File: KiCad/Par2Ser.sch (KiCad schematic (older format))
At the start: 34 parts, among them J1 DB25_Male, J2 Arduino UART header, J3 USB_C_Receptacle_USB2.0, J4 Conn_01x02, Q1 BC857, U1 Arduino_Nano_V3, U2 FT232RNL-REEL, U3 SC16IS750IBS,128, X1 Abracon-ASFL1-7.3728MHZ-EK-T

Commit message: Add LC4032V-5TN48C CPLD and remove Arduino Nano
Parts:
- removed JP1: PinHeader for 2mm Shunt Jumper, Connector_PinHeader_2.00mm:PinHeader_1x02_P2.00mm_Vertical, symbol Connector_Generic:Conn_01x02
- removed U1: Arduino_Nano_V3, Par2Ser:Arduino_Nano_V3, symbol Par2Ser:Arduino_Nano_V3
- added U4: LC4032V-5TN48C, Package_QFP:TQFP-48_7x7mm_P0.5mm, symbol Par2Ser:LC4032V-5TN48C
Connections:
- net labels added: 1V8, TCK, TD0, TDI, TMS
- net labels removed: Amiga_RESET
- wire segments 75 -> 73
- no-connect marks 26 -> 20
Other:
- moved on the sheet: C3, C4, C5, C6, C7, R6, RN1, RN2, U2

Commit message: Remove unused components and begin pin assigment on CPLD, place and route pull-up resistor networks and series resistor networks for parallel port signals
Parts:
- removed J2: Arduino UART header, Par2Ser:PinSocket_1x02_P2.54mm_SMD, symbol Connector_Generic:Conn_01x02
- removed J4: Conn_01x02, Par2Ser:PinSocket_1x02_P2.54mm_SMD, symbol Connector_Generic:Conn_01x02
- removed Q1: BC857, Package_TO_SOT_SMD:SOT-23_Handsoldering, symbol Transistor_BJT:BC857
- removed R5: 4k7, Resistor_SMD:R_1206_3216Metric_Pad1.30x1.75mm_HandSolder, symbol Device:R_Small
- removed RN2: 10k, Resistor_THT:R_Array_SIP9, symbol Device:R_Network08
- removed U3: SC16IS750IBS,128, Par2Ser:HVQFN-24-1EP_4x4mm_P0.5mm_EP2.6x2.6mm_HandSolder, symbol Par2Ser:SC16IS750IBS,128
- removed X1: Abracon-ASFL1-7.3728MHZ-EK-T, Oscillator:Oscillator_SMD_SeikoEpson_SG8002LB-4Pin_5.0x3.2mm, symbol Par2Ser:Abracon-ASFL1-7.3728MHZ-EK-T
- added RN2: 10k, Resistor_THT:R_Array_SIP5, symbol Device:R_Network04
- added RN3, RN4, RN5: 330, Resistor_SMD:R_Array_Convex_4x0603, symbol Device:R_Pack04
- added U3: FT240XS-R, Par2Ser:SOP64P599X175-24N, symbol Par2Ser:FT240XS-R
- R6: value 1k 0805 -> 330
- renumbered J3 to J2, U4 to U1
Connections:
- net labels added: BUSY_B9, D0_3V3, D0_B0, D1_3V3, D1_B1, D2_3V3, D2_B2, D3_3V3, D3_B3, D4_3V3, D4_B4, D5_3V3, D5_B5, D6_3V3, D6_B6, D7_3V3, D7_B7, POUT_B10, SELECT_B11, STRB
- net labels removed: 1V8, 7M, Base, Collector, MISO, MOSI, RX0, SCK, SS, TX0
- wire segments 73 -> 70
- no-connect marks 20 -> 16
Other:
- note removed: "Bottom"
- note removed: "Top"
- moved on the sheet: C3, C4, C5, C6, C7, D1, R1, R6, U2

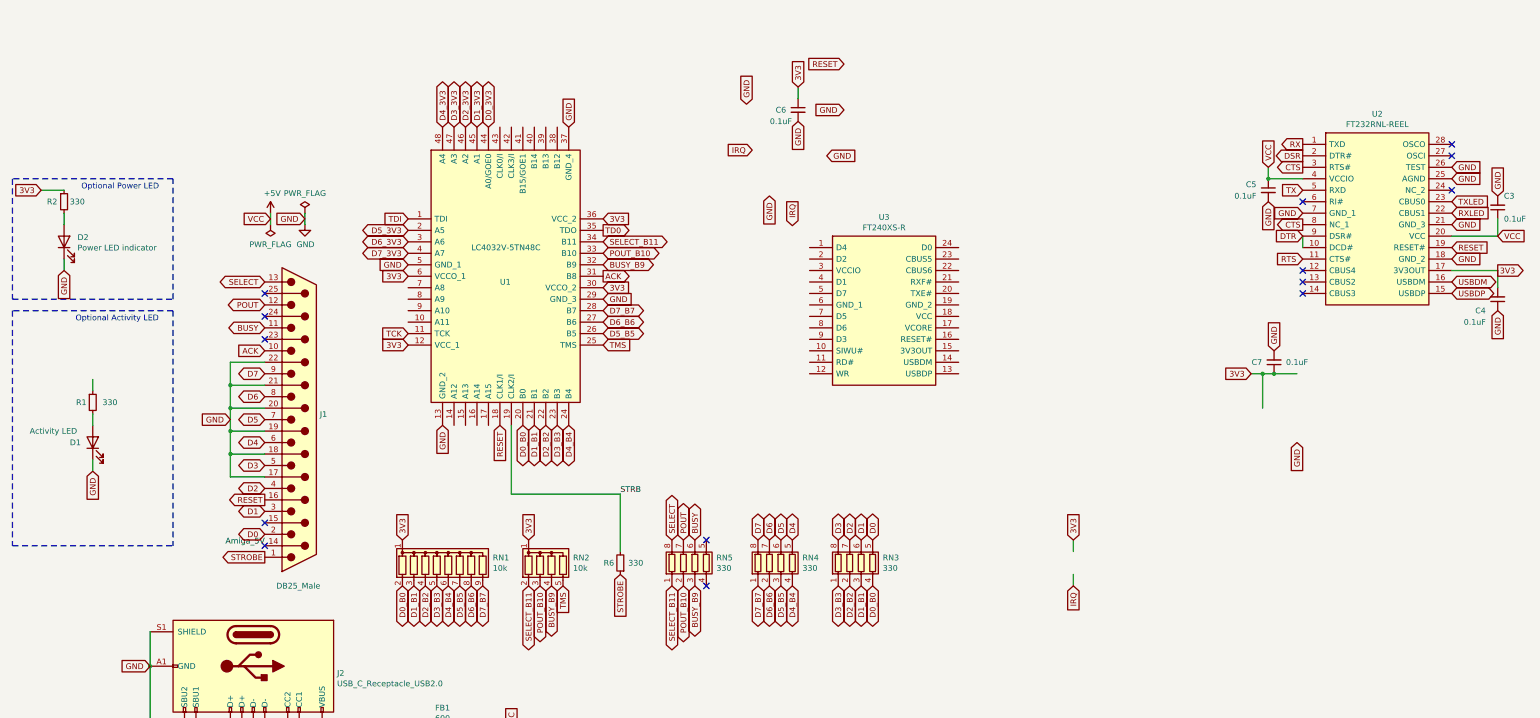
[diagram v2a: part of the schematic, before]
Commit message: Replace FT232RNL with FT240X and do some routing
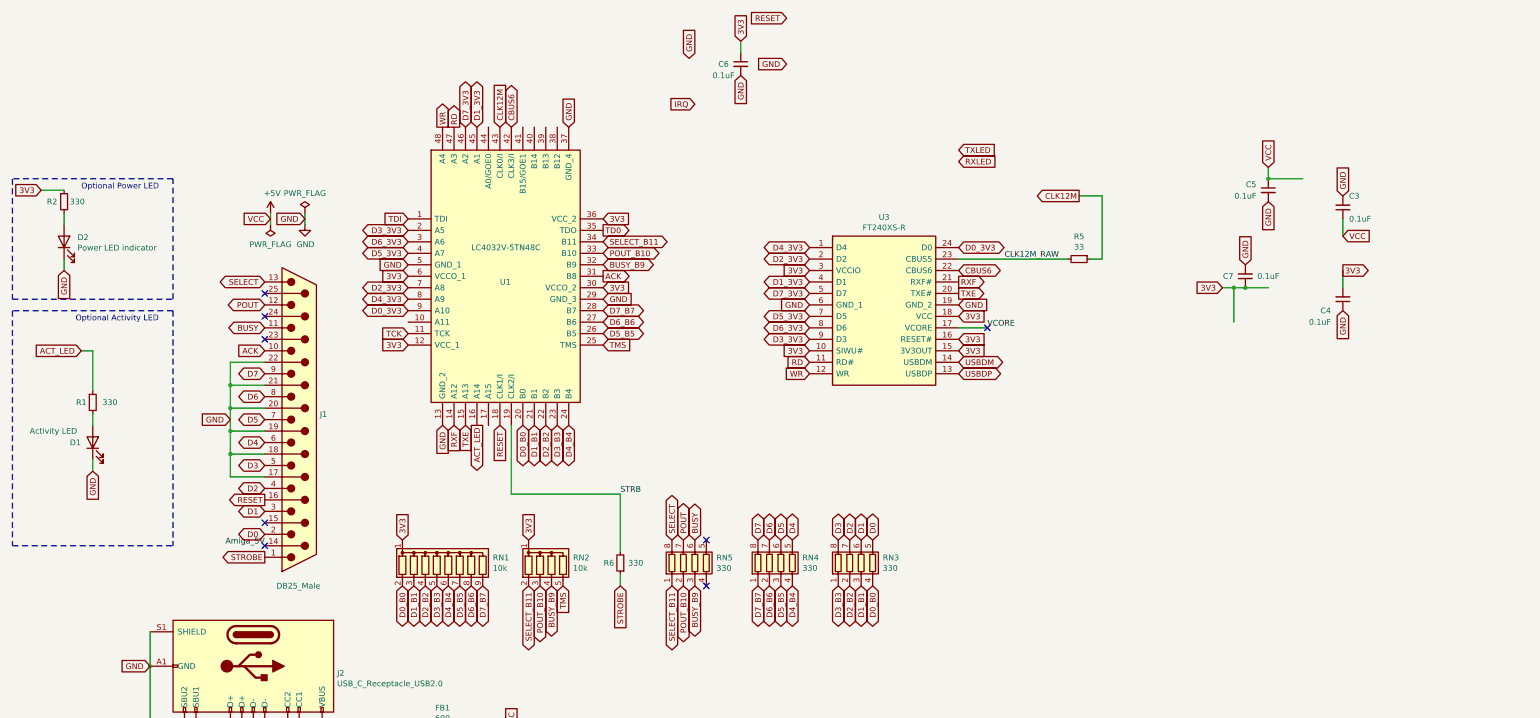
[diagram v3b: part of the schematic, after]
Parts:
- removed U2: FT232RNL-REEL, Package_SO:SSOP-28_5.3x10.2mm_P0.65mm, symbol Par2Ser:FT232RNL-REEL
- added R5: 33, Resistor_SMD:R_0603_1608Metric_Pad0.98x0.95mm_HandSolder, symbol Device:R_Small
- U3: footprint Par2Ser:SOP64P599X175-24N -> Package_SO:SSOP-24_3.9x8.7mm_P0.635mm
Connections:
- net labels added: ACT_LED, CBUS6, CLK12M, CLK12M_RAW, RD, RXF, TXE, VCORE, WR
- net labels removed: CTS, DSR, DTR, RTS, RX, TX
- wire segments 70 -> 72
- no-connect marks 16 -> 10
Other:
- moved on the sheet: C3, C4, C6, C7

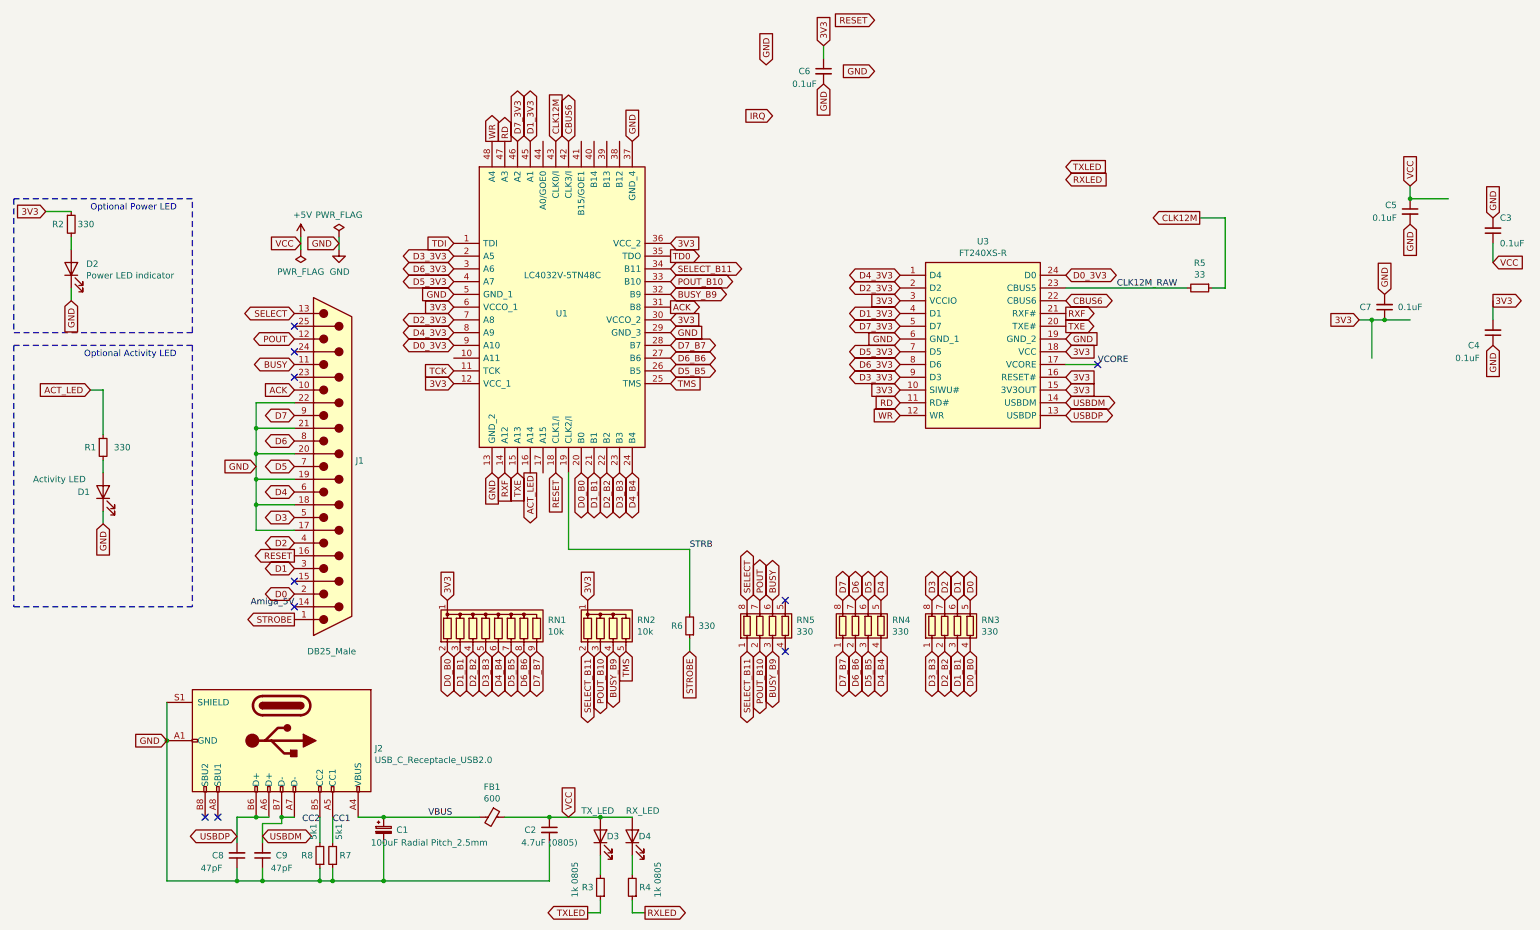
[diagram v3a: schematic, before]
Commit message: Fix placement and routing of caps and resistors
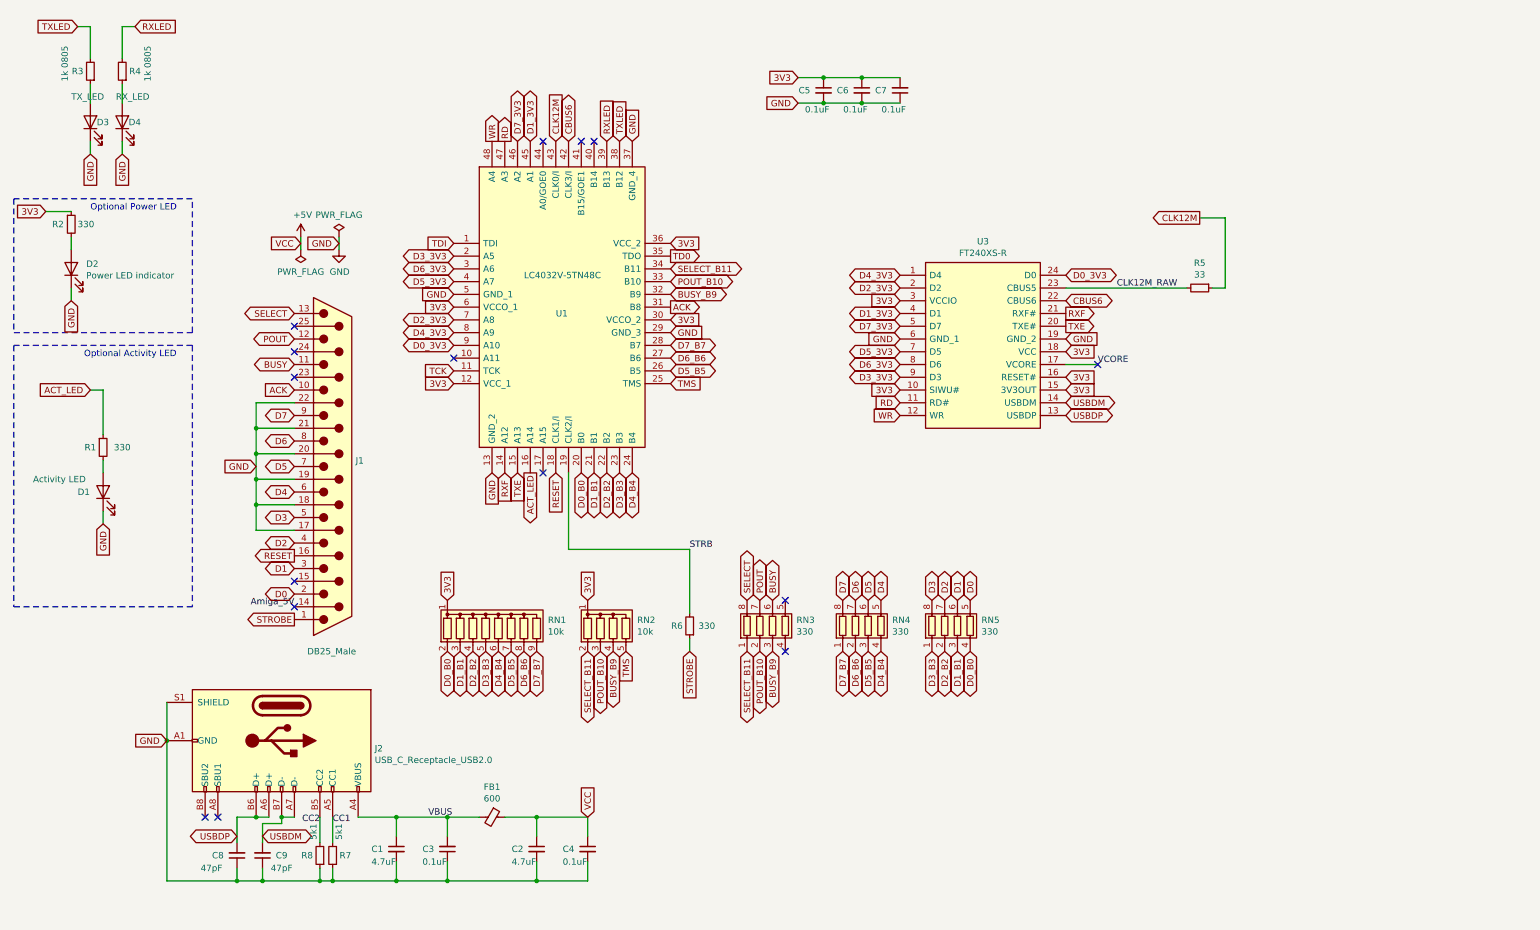
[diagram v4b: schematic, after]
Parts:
- removed C1: 100uF Radial Pitch_2.5mm, Capacitor_THT:CP_Radial_D5.0mm_P2.50mm, symbol Device:CP_Small
- added C1: 4.7uF, Capacitor_SMD:C_0805_2012Metric_Pad1.18x1.45mm_HandSolder, symbol Device:C_Small
- C2: value 4.7uF (0805) -> 4.7uF
- C6: footprint Capacitor_SMD:C_0805_2012Metric_Pad1.18x1.45mm_HandSolder -> Capacitor_SMD:C_0603_1608Metric_Pad1.08x0.95mm_HandSolder
- R1, R2, R7, R8: footprint Resistor_SMD:R_1206_3216Metric_Pad1.30x1.75mm_HandSolder -> Resistor_SMD:R_0805_2012Metric_Pad1.20x1.40mm_HandSolder
- renumbered C4 to C3, C5 to C4, C3 to C5, RN5 to RN3, RN3 to RN5
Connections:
- net labels removed: IRQ
- wire segments 72 -> 79
- no-connect marks 10 -> 15
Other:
- moved on the sheet: C2, C3, C4, C5, C6, C7, D3, D4, R3, R4

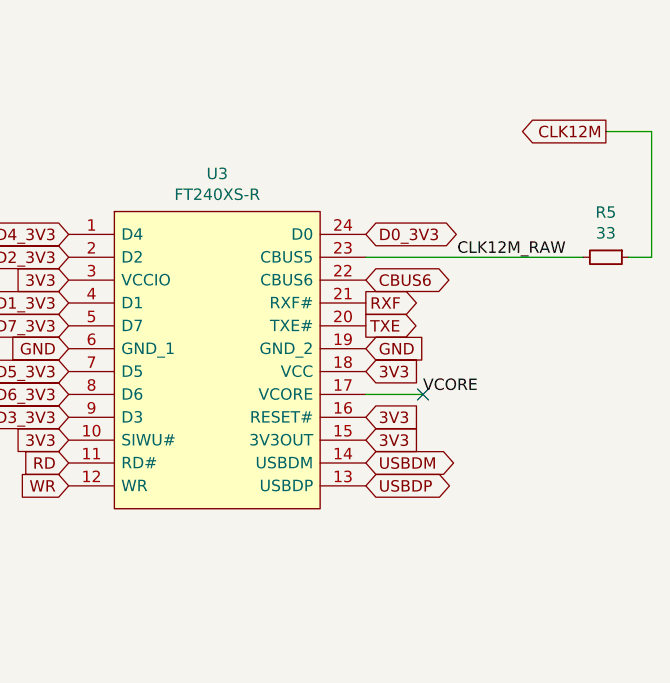
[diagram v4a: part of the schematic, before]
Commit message: Add resistors on the two USB data lines
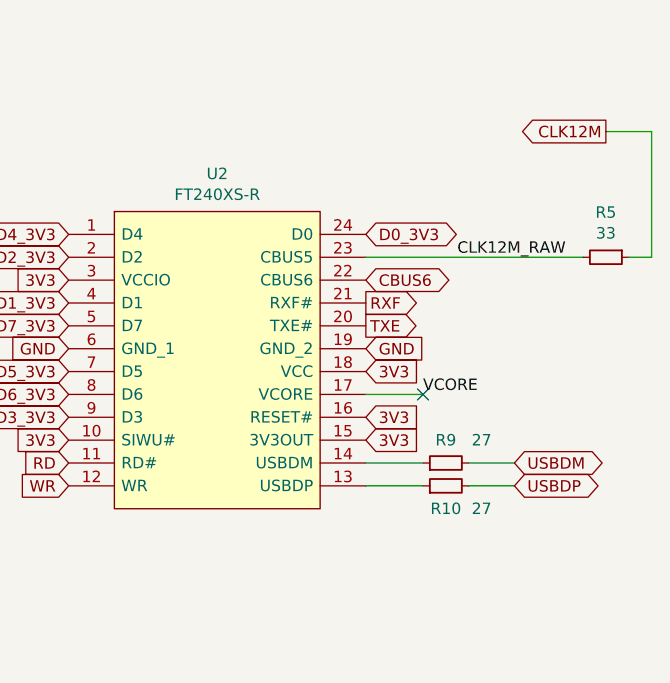
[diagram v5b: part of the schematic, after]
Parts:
- added R10, R9: 27, Resistor_SMD:R_0805_2012Metric_Pad1.20x1.40mm_HandSolder, symbol Device:R_Small
- renumbered U3 to U2
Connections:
- net USBDM: now also R9.2; no longer U2.14 (USBDM)
- net USBDP: now also R10.2; no longer U2.13 (USBDP)
- new net: R10.1, U2.13 (USBDP)
- new net: R9.1, U2.14 (USBDM)
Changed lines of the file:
@@
 D7_3V3
 $Comp
-L Par2Ser:FT240XS-R U3
+L Par2Ser:FT240XS-R U2
 U 1 1 6A22D05C
 P 9150 3250
-F 0 "U3" H 9150 4065 50  0000 C CNN
+F 0 "U2" H 9150 4065 50  0000 C CNN
 F 1 "FT240XS-R" H 9150 3974 50  0000 C CNN
 F 2 "Package_SO:SSOP-24_3.9x8.7mm_P0.635mm" H 8900 3950 50  0001 L CNN
@@
 Text GLabel 9800 3200 2    50   Input ~ 0
 GND
-Text GLabel 9800 3700 2    50   BiDi ~ 0
+Text GLabel 10450 3700 2    50   BiDi ~ 0
 USBDM
-Text GLabel 9800 3800 2    50   BiDi ~ 0
+Text GLabel 10450 3800 2    50   BiDi ~ 0
 USBDP
 Text GLabel 9800 3600 2    50   Input ~ 0
@@
 Wire Wire Line
 	2400 1200 2400 1350
+$Comp
+L Device:R_Small R10
+U 1 1 6A5B4EB2
+P 10150 3800
+F 0 "R10" V 10050 3800 50  0000 C CNN
+F 1 "27" V 10050 3600 50  0000 L CNN
+F 2 "Resistor_SMD:R_0805_2012Metric_Pad1.20x1.40mm_HandSolder" H 10150 3800 50  0001 C CNN
+F 3 "~" H 10150 3800 50  0001 C CNN
+	1    10150 3800
+	0    -1   -1   0
+$EndComp
+$Comp
+L Device:R_Small R9
+U 1 1 6A5B195C
+P 10150 3700
+F 0 "R9" V 10250 3700 50  0000 C CNN
+F 1 "27" V 10250 3500 50  0000 L CNN
+F 2 "Resistor_SMD:R_0805_2012Metric_Pad1.20x1.40mm_HandSolder" H 10150 3700 50  0001 C CNN
+F 3 "~" H 10150 3700 50  0001 C CNN
+	1    10150 3700
+	0    -1   -1   0
+$EndComp
+Wire Wire Line
+	10050 3700 9800 3700
+Wire Wire Line
+	10050 3800 9800 3800
+Wire Wire Line
+	10450 3700 10250 3700
+Wire Wire Line
+	10450 3800 10250 3800
 $EndSCHEMATC
